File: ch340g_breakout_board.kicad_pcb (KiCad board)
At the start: 2 copper layers, 24.1 x 20.3 mm, 6 parts, among them J1 Conn_01x08_Male, J2 Conn_01x08_Male, U1 CH340G, Y1 12Mhz

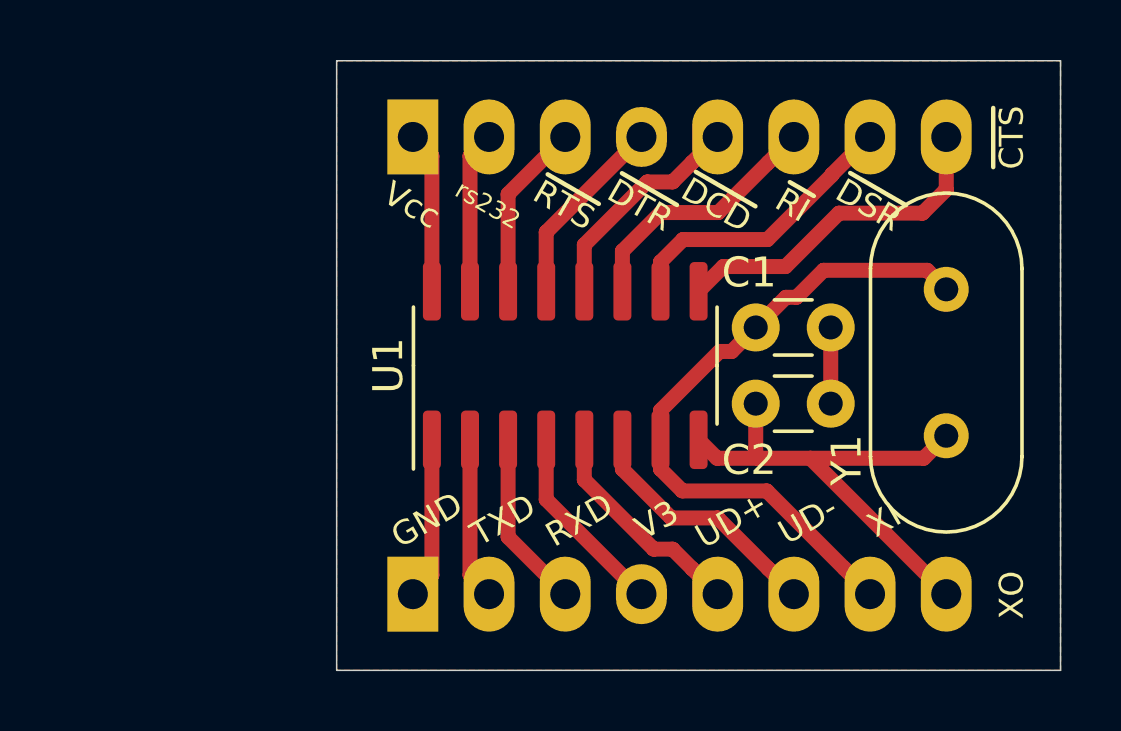
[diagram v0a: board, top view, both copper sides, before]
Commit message: Updated to REV2: Includes USB-Mini B connector
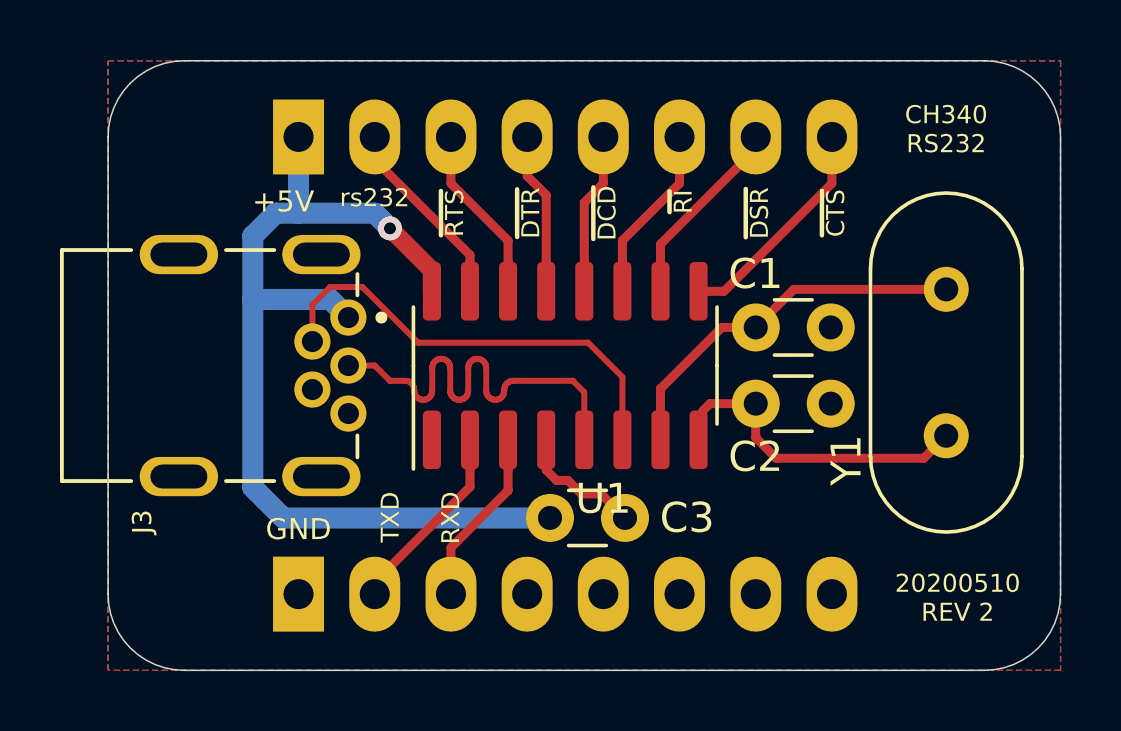
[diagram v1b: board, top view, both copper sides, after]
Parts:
- added C3: 10n, Capacitor_THT:C_Disc_D3.0mm_W1.6mm_P2.50mm, F.Cu at (134.1, 106.7)
- added J3: XM7D-0512, Personal:OMRON_XM7D-0512, F.Cu at (126.5, 101.6)
- added REF**: OSHW-Logo2_7.3x6mm_SilkScreen, Symbol:OSHW-Logo2_7.3x6mm_SilkScreen, B.Cu at (134.5, 100.2)
- moved J1 3.81 mm to (125.7, 94.0)
- moved J2 3.81 mm to (125.7, 109.2)
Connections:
- J2 pad 4: /V3 -> Net-(J2-Pad4)
- J2 pad 5: /UD+ -> Net-(J2-Pad5)
- J2 pad 6: /UD- -> Net-(J2-Pad6)
- J2 pad 7: /XI -> Net-(J2-Pad7)
- J2 pad 8: /XO -> Net-(J2-Pad8)
- U1 pad 4: /V3 -> Net-(C3-Pad2)
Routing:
- net /Vcc: track 5.41 -> 32.5 mm, vias 0 -> 1
- net /XI: track 22.4 -> 12.6 mm
- net /GND: track 7.95 -> 0.00 mm
- net /UD+: track 7.36 -> 15.0 mm
- net /UD-: track 8.42 -> 15.1 mm
- net /XO: track 17.1 -> 10.5 mm
- net /V3: track 6.47 -> 0.00 mm
- net Net-(C3-Pad2): track 0.00 -> 4.30 mm
- net /~CTS: track 11.4 -> 7.48 mm
- net /~DSR: track 9.70 -> 6.46 mm
- net /~RI: track 8.63 -> 5.93 mm
- net /~DCD: track 7.55 -> 5.41 mm
- net /~DTR: track 6.46 -> 5.41 mm
- net /TXD: track 5.41 -> 6.46 mm
- net /RS232: track 5.41 -> 6.46 mm
- added copper zone on B.Cu, net /GND
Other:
- board size 24.1 x 20.3 mm -> 31.8 x 20.3 mm
- net class Default: clearance 0.4 -> 0.3; trace_width 0.5 -> 0.3
- net class narrow spacings added: clearance 0.2, trace_width 0.3, via_dia 0.8, via_drill 0.4
- rule trace_clearance: 0.4 -> 0.3
- rule via_min_size: 0.4 -> 0.45
- board text added: "+5V"
- board text added: "20200510 REV 2"
- board text added: "CH340 Breakout Board"
- board text added: "CH340 RS232"
- board text added: "© 2020 Jaap Geurts"
- board text removed: "UD+"
- board text removed: "UD-"
- board text removed: "V3"
- board text removed: "Vcc"
- board text removed: "XI"
- board text removed: "XO"

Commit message: Revision 2
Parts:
- moved Y1 1.53 mm to (145.8, 99.2)
- moved REF** 1.14 mm to (134.5, 99.1)
- moved C1 0.80 mm to (141.2, 101.1), turned to 90 degrees
- moved C2 0.57 mm to (141.2, 103.4), turned to 270 degrees
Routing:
- net /XO: track 10.5 -> 7.31 mm
- net /XI: track 12.6 -> 10.6 mm
- net /GND: vias 0 -> 5
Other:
- board size 31.8 x 20.3 mm -> 30 x 20.3 mm
- board text added: "MAY '20 REV 2"
- board text removed: "20200510 REV 2"
